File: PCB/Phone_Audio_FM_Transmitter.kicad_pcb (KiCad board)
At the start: 2 copper layers, 92.7 x 61 mm, 51 parts, among them J1 Vin, J2 Conn_Coaxial, J3 Conn_Coaxial, J4 USB_B_Micro, J5 Test Point, SW1 SW_Push, SW2 SW_Push, SW3 SW_Push, SW4 SW_Push, U1 TPS5403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

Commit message: Finished Rev. 1 layout with Gerber files
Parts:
- added J6: Rec, Connector_Molex:Molex_KK-254_AE-6410-02A_1x02_P2.54mm_Vertical, F.Cu at (195.6, 66.0)
- added J7: Trans, Connector_Molex:Molex_KK-254_AE-6410-02A_1x02_P2.54mm_Vertical, F.Cu at (195.6, 76.2)
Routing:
- net Net-(J2-In): track 10.5 -> 20.3 mm
- net Net-(J3-In): track 10.4 -> 19.8 mm
- net /USB_D+: track 42.5 -> 41.8 mm
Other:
- board text added: "Team 18 Board Rev. 1 03-08-23"

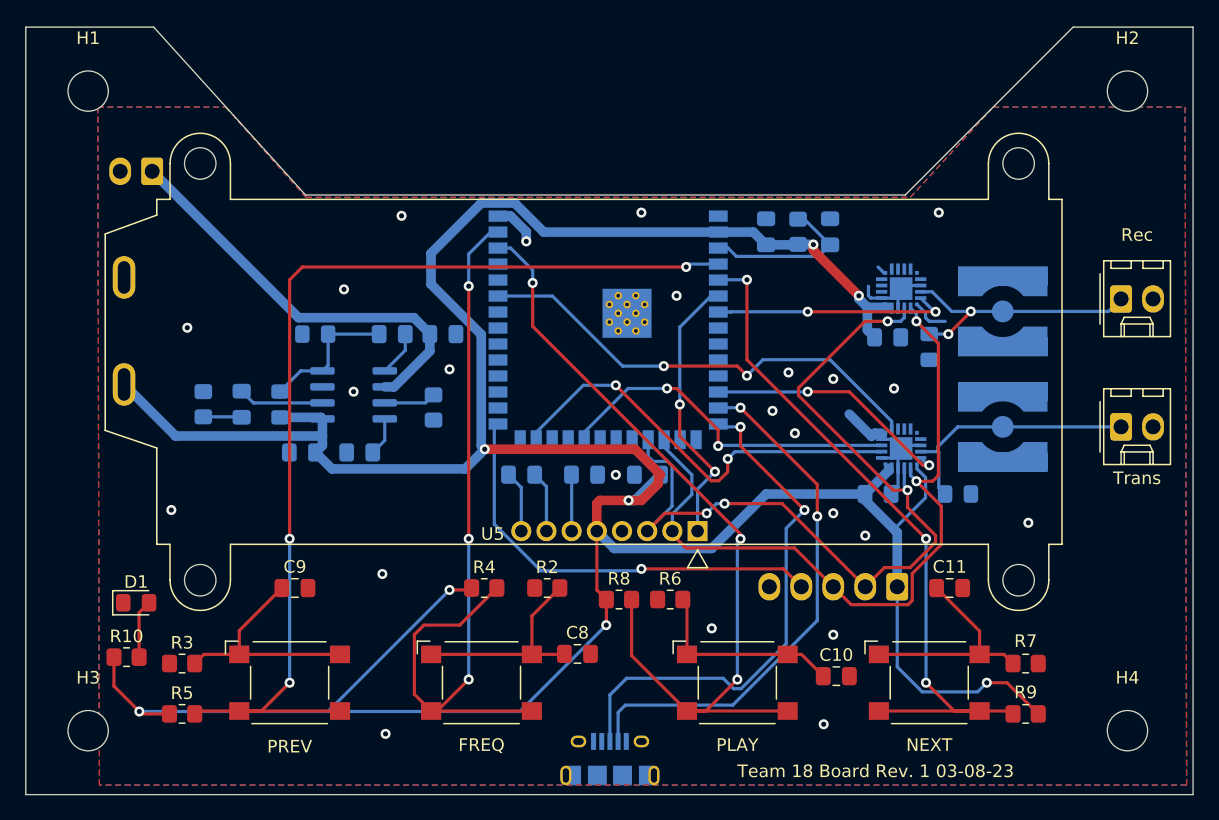
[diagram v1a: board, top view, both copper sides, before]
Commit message: Completed PCB Rev 2. Changed microcontroller to ESP32-WROOM-32, added UART bridge, removed button pull-up resistors, added I2S test point, added option to control backlight, and better organized all traces
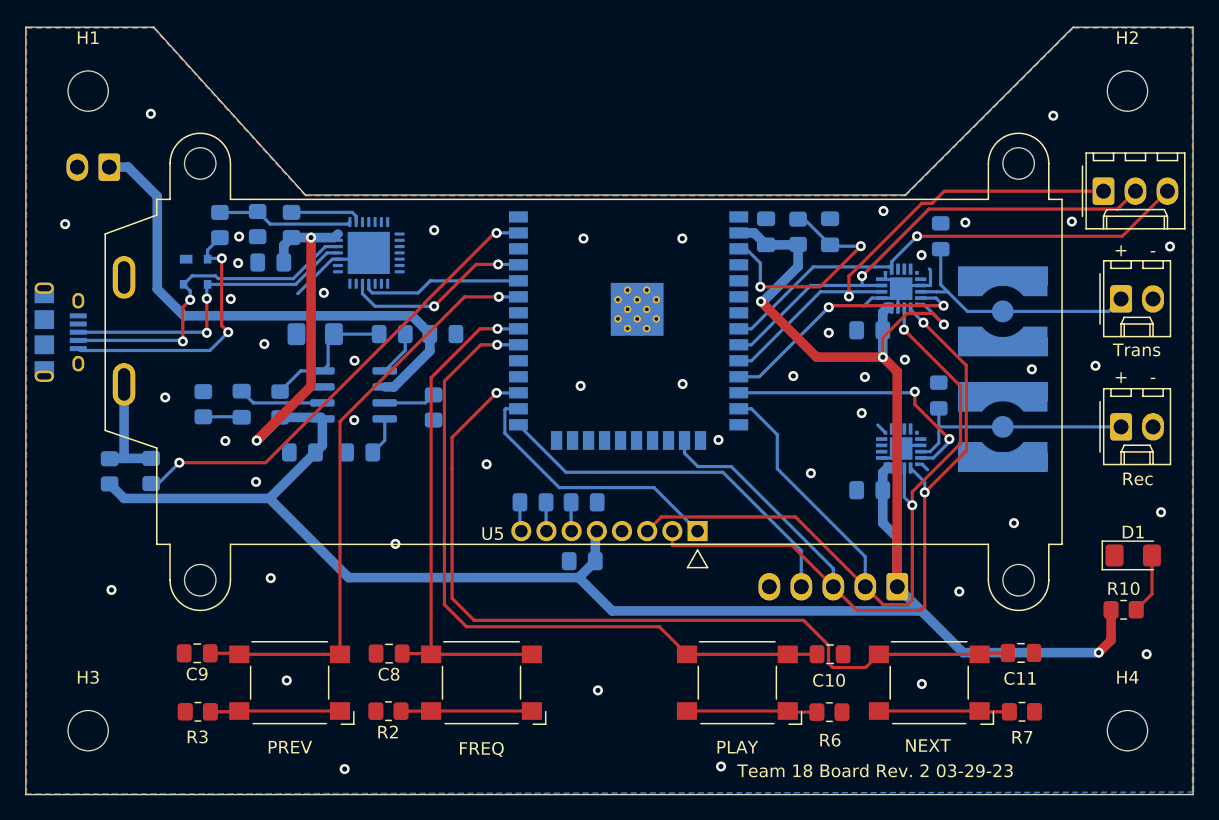
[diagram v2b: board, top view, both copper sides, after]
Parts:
- removed R4, R5, R8, R9: 100k, Resistor_SMD:R_0805_2012Metric_Pad1.20x1.40mm_HandSolder
- removed U4: ESP32-S3-WROOM-1, RF_Module:ESP32-S3-WROOM-1
- added C17: 10uF, Capacitor_SMD:C_0805_2012Metric_Pad1.18x1.45mm_HandSolder, B.Cu at (128.0, 63.1)
- added D3: SP0503BAHT, Package_TO_SOT_SMD:SOT-143, B.Cu at (122.1, 63.9)
- added J8: I2S Test Point, Connector_Molex:Molex_KK-254_AE-6410-03A_1x03_P2.54mm_Vertical, F.Cu at (194.2, 57.5)
- added R13: 1k, Resistor_SMD:R_0805_2012Metric_Pad1.20x1.40mm_HandSolder, B.Cu at (129.7, 60.2)
- added R14: 22.1k, Resistor_SMD:R_0805_2012Metric_Pad1.20x1.40mm_HandSolder, B.Cu at (124.0, 60.2)
- added R15: 47.5k, Resistor_SMD:R_0805_2012Metric_Pad1.20x1.40mm_HandSolder, B.Cu at (127.0, 60.1)
- added R16: 100, Resistor_SMD:R_0805_2012Metric_Pad1.20x1.40mm_HandSolder, B.Cu at (115.2, 79.7)
- added R17: 100, Resistor_SMD:R_0805_2012Metric_Pad1.20x1.40mm_HandSolder, B.Cu at (118.5, 79.7)
- added U6: ESP32-WROOM-32, RF_Module:ESP32-WROOM-32, B.Cu at (156.5, 67.8)
- added U7: CP2102N-Axx-xQFN28, Package_DFN_QFN:QFN-28-1EP_5x5mm_P0.5mm_EP3.35x3.35mm, B.Cu at (135.8, 62.4)
- D1: footprint LED_SMD:LED_0805_2012Metric_Pad1.15x1.40mm_HandSolder -> LED_SMD:LED_1206_3216Metric_Pad1.42x1.75mm_HandSolder
- D2: footprint Diode_SMD:D_0805_2012Metric_Pad1.15x1.40mm_HandSolder -> Diode_SMD:D_1206_3216Metric_Pad1.42x1.75mm_HandSolder
- moved D1 79.3 mm to (196.5, 86.4)
- moved R10 79.3 mm to (195.8, 90.7)
- moved J4 55.3 mm to (111.4, 68.7), turned to 90 degrees
- moved L2 20.5 mm to (181.3, 61.1), turned to -90 degrees
- moved R2 16.0 mm to (137.4, 98.8)
- moved R6 15.5 mm to (172.4, 98.9), turned to 180 degrees
- moved C8 15.0 mm to (137.4, 94.2), turned to 180 degrees
- moved C2 13.0 mm to (175.6, 68.5), turned to 0 degrees
- moved U2 12.7 mm to (178.1, 77.9)
- moved U3 12.7 mm to (178.1, 65.2)
- moved C1 12.2 mm to (175.6, 81.2), turned to 0 degrees
- moved J6 10.2 mm to (195.6, 76.2)
- moved J7 10.2 mm to (195.6, 66.0)
- moved C9 9.33 mm to (122.2, 94.2), turned to 180 degrees
- moved J2 9.17 mm to (186.2, 76.2)
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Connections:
- C10 pad 1: Net-(C10-Pad1) -> /User Interface/PLAY/PAUSE
- C11 pad 1: Net-(C11-Pad1) -> /User Interface/NEXT
- C8 pad 1: Net-(C8-Pad1) -> /User Interface/CHANGE_FREQ
- C9 pad 1: Net-(C9-Pad1) -> /User Interface/PREV
- J4 pad 1: unconnected-(J4-VBUS-Pad1) -> Net-(J4-VBUS)
- J4 pad 2: /USB_D- -> Net-(J4-D-)
- J4 pad 3: /USB_D+ -> Net-(J4-D+)
- R2 pad 2: Net-(C8-Pad1) -> Net-(R2-Pad2)
- R3 pad 2: Net-(C9-Pad1) -> Net-(R3-Pad2)
- R6 pad 2: Net-(C10-Pad1) -> Net-(R6-Pad2)
- R7 pad 2: Net-(C11-Pad1) -> Net-(R7-Pad2)
- SW1 pad 1: Net-(C8-Pad1) -> Net-(R2-Pad2)
- SW2 pad 1: Net-(C9-Pad1) -> Net-(R3-Pad2)
- SW3 pad 1: Net-(C10-Pad1) -> Net-(R6-Pad2)
- SW4 pad 1: Net-(C11-Pad1) -> Net-(R7-Pad2)
- U5 pad 9: +3.3V -> Net-(U5-A)
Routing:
- net +3.3V: track 259.0 -> 199.1 mm, vias 8 -> 6
- net /USB_D-: track 42.4 -> 0.00 mm, vias 2 -> 0
- net /USB_D+: track 41.8 -> 0.00 mm, vias 2 -> 0
- net /User Interface/LCD_BKLT: track 0.00 -> 37.5 mm, vias 0 -> 2
- net /User Interface/PREV: track 83.1 -> 47.1 mm, vias 3 -> 1
- net Net-(J4-D-): track 0.00 -> 27.0 mm, vias 0 -> 2
- net Net-(J4-D+): track 0.00 -> 25.5 mm, vias 0 -> 2
- net /User Interface/CHANGE_FREQ: track 63.6 -> 40.8 mm, vias 3 -> 1
- net Net-(J4-VBUS): track 0.00 -> 21.9 mm, vias 0 -> 2
- net Net-(C9-Pad1): track 18.5 -> 0.00 mm
- net Net-(C11-Pad1): track 17.6 -> 0.00 mm
- net Net-(C8-Pad1): track 16.8 -> 0.00 mm
- net Net-(C10-Pad1): track 16.0 -> 0.00 mm
- net /TXDO: track 0.00 -> 15.0 mm, vias 0 -> 2
- net /RXDO: track 0.00 -> 12.8 mm
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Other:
- board text added: "B"
- board text added: "D"
- board text added: "GND"
- board text added: "LR"
- board text added: "SCL"
- board text added: "SDA"
- board text added: "Team 18 Board Rev. 2 03-29-23"
- board text added: "VDD"
- board text removed: "Team 18 Board Rev. 1 03-08-23"

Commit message: Added resistors to I2S pins on transmitter
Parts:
- added R4: 600, Resistor_SMD:R_0805_2012Metric_Pad1.20x1.40mm_HandSolder, B.Cu at (173.6, 65.1)
- added R5: 2k, Resistor_SMD:R_0805_2012Metric_Pad1.20x1.40mm_HandSolder, B.Cu at (184.4, 59.4)
- added R8: 2k, Resistor_SMD:R_0805_2012Metric_Pad1.20x1.40mm_HandSolder, B.Cu at (179.9, 59.4)
- moved L2 11.5 mm to (192.3, 64.4)
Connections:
- U3 pad 13: /I2S_DATA -> Net-(U3-DIN)
- U3 pad 14: /I2S_LRCLK -> Net-(U3-DFS)
- U3 pad 17: /I2S_BCLK -> Net-(U3-GPO3/DCLK)
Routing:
- net Net-(U3-DFS): track 0.00 -> 14.7 mm, vias 0 -> 2
- net Net-(U3-GPO3/DCLK): track 0.00 -> 4.93 mm
- net /I2S_BCLK: track 39.1 -> 41.3 mm, vias 1 -> 0
- net Net-(J3-In): track 20.6 -> 18.6 mm
- net Net-(U3-DIN): track 0.00 -> 1.92 mm
- net /I2S_DATA: track 38.5 -> 37.3 mm
- net /I2S_LRCLK: track 38.6 -> 38.0 mm, vias 1 -> 2
- net GND: vias 45 -> 47

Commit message: Added crystal oscillator for receiver IC and RCLK from ESP32 to FM ICs
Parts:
- added C18: 22pF, Capacitor_SMD:C_0805_2012Metric_Pad1.18x1.45mm_HandSolder, B.Cu at (170.6, 78.3)
- added C19: 22pF, Capacitor_SMD:C_0805_2012Metric_Pad1.18x1.45mm_HandSolder, B.Cu at (172.6, 78.3)
- added R9: 0, Resistor_SMD:R_0805_2012Metric_Pad1.20x1.40mm_HandSolder, B.Cu at (183.2, 84.7)
- added Y1: 32.768kHz, Crystal:Crystal_SMD_2012-2Pin_2.0x1.2mm_HandSoldering, B.Cu at (171.7, 75.2)
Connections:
- U2 pad 17: unconnected-(U2-GPO3/DCLK-Pad17) -> /RGPO3
- U2 pad 9: GND -> /RRCLK
- U3 pad 9: GND -> /TRCLK
- U6 pad 28: unconnected-(U6-IO17-Pad28) -> /TRCLK
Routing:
- net /TRCLK: track 0.00 -> 79.3 mm, vias 0 -> 3
- net /RRCLK: track 0.00 -> 38.9 mm, vias 0 -> 4
- net /RGPO3: track 0.00 -> 8.23 mm
- net GND: track 27.9 -> 20.0 mm, vias 47 -> 48
- net +3.3V: track 199.1 -> 201.9 mm
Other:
- board text added: "Team 18 Board Rev. 2.1 04-10-23"
- board text removed: "Team 18 Board Rev. 2 03-29-23"
